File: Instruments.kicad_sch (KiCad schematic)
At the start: 1 part

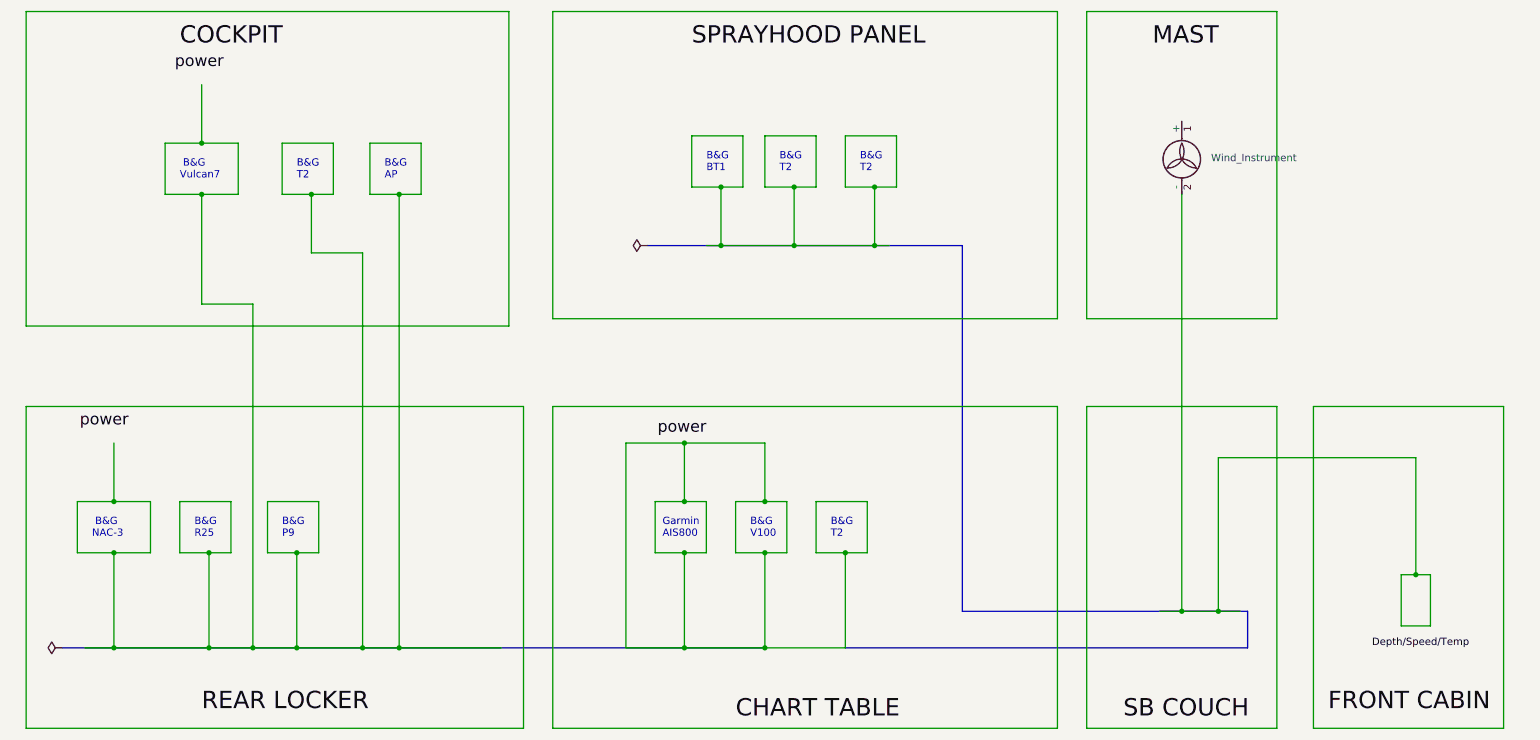
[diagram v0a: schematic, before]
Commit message: BMS Monitor added to network
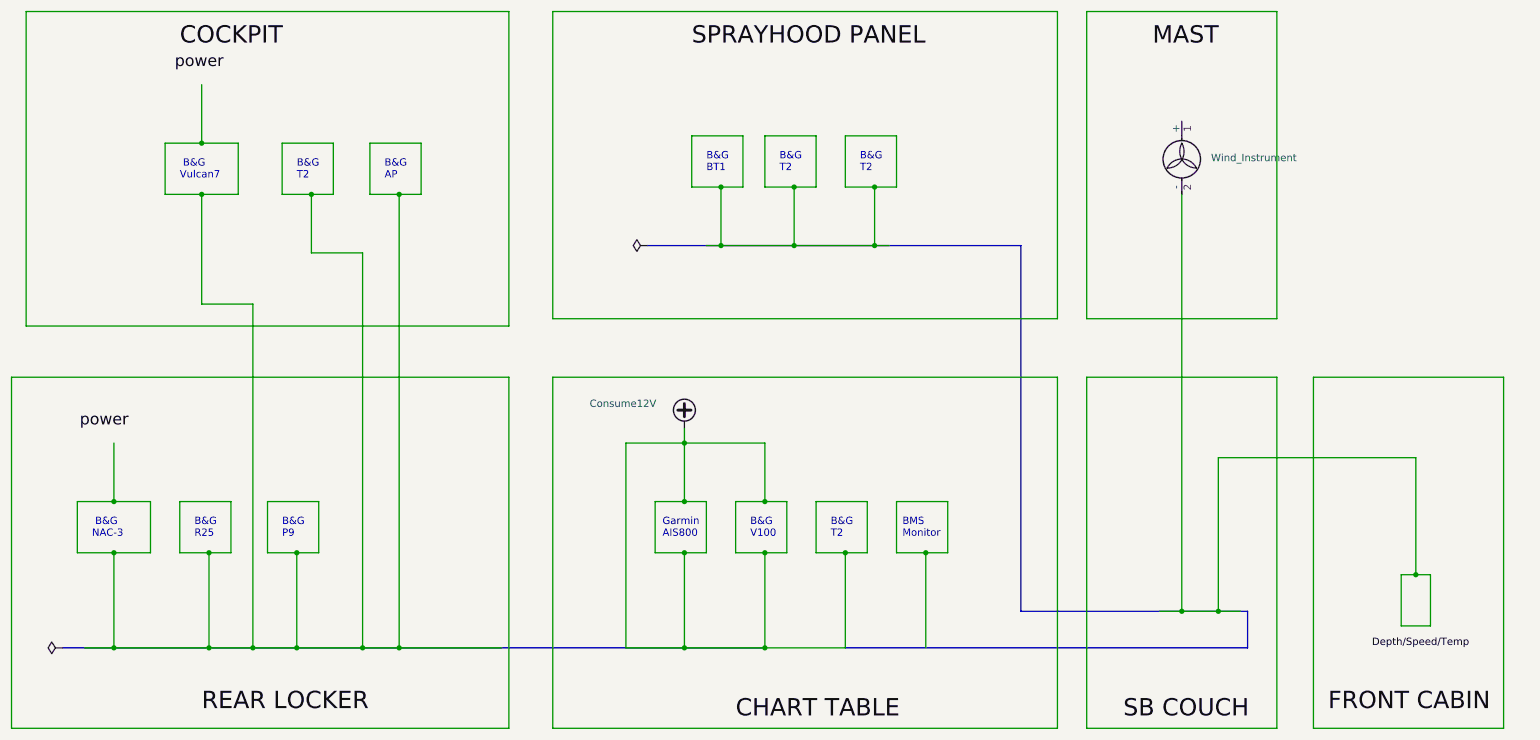
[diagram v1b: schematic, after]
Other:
- note added: "BMS Monitor"
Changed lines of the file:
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@@
 	(title_block
 		(title "Frk Jensen - Instrument cabling")
-		(rev "1.0")
+		(date "2025-06-08")
+		(rev "1.1")
 	)
 	(junction
@@
 	)
 	(junction
+		(at 180.34 115.57)
+		(diameter 0)
+		(color 0 0 0 0)
+	)
+	(junction
 		(at 71.12 115.57)
 		(diameter 0)
@@
 	(wire
 		(pts
+			(xy 175.26 115.57) (xy 180.34 115.57)
+		)
+		(stroke
+			(width 0.4)
+			(type default)
+			(color 1 0 0 1)
+		)
+	)
+	(wire
+		(pts
 			(xy 55.88 115.57) (xy 55.88 132.08)
 		)
@@
 	(bus
 		(pts
-			(xy 186.69 125.73) (xy 186.69 62.23)
+			(xy 196.85 125.73) (xy 196.85 62.23)
 		)
 		(stroke
@@
 	(bus
 		(pts
-			(xy 186.69 125.73) (xy 224.79 125.73)
+			(xy 196.85 125.73) (xy 224.79 125.73)
 		)
 		(stroke
@@
 	(wire
 		(pts
-			(xy 110.49 146.05) (xy 110.49 90.17)
-		)
-		(stroke
-			(width 0)
-			(type dot)
-			(color 0 0 255 1)
+			(xy 107.95 146.05) (xy 107.95 85.09)
+		)
+		(stroke
+			(width 0)
+			(type dot)
+			(color 0 0 255 1)
+		)
+	)
+	(wire
+		(pts
+			(xy 138.43 93.98) (xy 138.43 96.52)
+		)
+		(stroke
+			(width 0)
+			(type default)
 		)
 	)
@@
 	(wire
 		(pts
-			(xy 115.57 90.17) (xy 203.2 90.17)
+			(xy 115.57 85.09) (xy 203.2 85.09)
 		)
 		(stroke
@@
 	(wire
 		(pts
-			(xy 208.28 90.17) (xy 208.28 146.05)
+			(xy 208.28 85.09) (xy 208.28 146.05)
 		)
 		(stroke
@@
 	(wire
 		(pts
-			(xy 203.2 146.05) (xy 203.2 90.17)
+			(xy 203.2 146.05) (xy 203.2 85.09)
 		)
 		(stroke
@@
 	(wire
 		(pts
+			(xy 180.34 115.57) (xy 180.34 132.08)
+		)
+		(stroke
+			(width 1)
+			(type default)
+		)
+	)
+	(wire
+		(pts
 			(xy 166.37 115.57) (xy 170.18 115.57)
 		)
@@
 	(wire
 		(pts
+			(xy 175.26 106.68) (xy 175.26 115.57)
+		)
+		(stroke
+			(width 0.4)
+			(type default)
+			(color 1 0 0 1)
+		)
+	)
+	(wire
+		(pts
 			(xy 208.28 74.93) (xy 241.3 74.93)
 		)
@@
 		)
 	)
+	(wire
+		(pts
+			(xy 175.26 106.68) (xy 184.15 106.68)
+		)
+		(stroke
+			(width 0.4)
+			(type default)
+			(color 1 0 0 1)
+		)
+	)
 	(bus
 		(pts
@@
 	(wire
 		(pts
-			(xy 24.13 146.05) (xy 110.49 146.05)
+			(xy 21.59 146.05) (xy 107.95 146.05)
 		)
 		(stroke
@@
 	(wire
 		(pts
-			(xy 280.67 146.05) (xy 280.67 90.17)
-		)
-		(stroke
-			(width 0)
-			(type dot)
-			(color 0 0 255 1)
-		)
-	)
-	(wire
-		(pts
-			(xy 247.65 90.17) (xy 280.67 90.17)
+			(xy 280.67 146.05) (xy 280.67 85.09)
+		)
+		(stroke
+			(width 0)
+			(type dot)
+			(color 0 0 255 1)
+		)
+	)
+	(wire
+		(pts
+			(xy 247.65 85.09) (xy 280.67 85.09)
 		)
 		(stroke
@@
 	(bus
 		(pts
-			(xy 171.45 62.23) (xy 186.69 62.23)
+			(xy 171.45 62.23) (xy 196.85 62.23)
 		)
 		(stroke
@@
 	(wire
 		(pts
-			(xy 24.13 90.17) (xy 24.13 146.05)
+			(xy 21.59 85.09) (xy 21.59 146.05)
 		)
 		(stroke
@@
 	(wire
 		(pts
-			(xy 247.65 90.17) (xy 247.65 146.05)
+			(xy 247.65 85.09) (xy 247.65 146.05)
 		)
 		(stroke
@@
 	(wire
 		(pts
-			(xy 208.28 90.17) (xy 241.3 90.17)
-		)
-		(stroke
-			(width 0)
-			(type dot)
-			(color 0 0 255 1)
-		)
-	)
-	(wire
-		(pts
-			(xy 24.13 90.17) (xy 110.49 90.17)
+			(xy 208.28 85.09) (xy 241.3 85.09)
+		)
+		(stroke
+			(width 0)
+			(type dot)
+			(color 0 0 255 1)
+		)
+	)
+	(wire
+		(pts
+			(xy 21.59 85.09) (xy 107.95 85.09)
 		)
 		(stroke
@@
 	(wire
 		(pts
+			(xy 184.15 106.68) (xy 184.15 115.57)
+		)
+		(stroke
+			(width 0.4)
+			(type default)
+			(color 1 0 0 1)
+		)
+	)
+	(wire
+		(pts
 			(xy 152.4 43.18) (xy 161.29 43.18)
 		)
@@
 	(wire
 		(pts
+			(xy 180.34 115.57) (xy 184.15 115.57)
+		)
+		(stroke
+			(width 0.4)
+			(type default)
+			(color 1 0 0 1)
+		)
+	)
+	(wire
+		(pts
 			(xy 265.43 119.38) (xy 267.97 119.38)
 		)
@@
 	(wire
 		(pts
-			(xy 115.57 90.17) (xy 115.57 146.05)
+			(xy 115.57 85.09) (xy 115.57 146.05)
 		)
 		(stroke
@@
 	(wire
 		(pts
-			(xy 241.3 146.05) (xy 241.3 90.17)
+			(xy 241.3 146.05) (xy 241.3 85.09)
 		)
 		(stroke
@@
 		)
 	)
+	(text "BMS\nMonitor"
+		(exclude_from_sim no)
+		(at 176.276 113.03 0)
+		(effects
+			(font
+				(size 1.27 1.27)
+			)
+			(justify left bottom)
+		)
+	)
 	(text "B&G\nT2"
 		(exclude_from_sim no)
@@
 			)
 			(justify left bottom)
-		)
-	)
-	(label "power"
-		(at 142.24 95.25 180)
-		(effects
-			(font
-				(size 2 2)
-			)
-			(justify right bottom)
 		)
 	)
@@
 					(unit 1)
 				)
+			)
+		)
+	)
+	(symbol
+		(lib_id "power:+VDC")
+		(at 138.43 93.98 0)
+		(unit 1)
+		(exclude_from_sim no)
+		(in_bom yes)
+		(on_board yes)
+		(dnp no)
+		(property "Reference" "#PWR1"
+			(at 138.43 96.52 0)
+			(effects
+				(font
+					(size 1.27 1.27)
+				)
+				(hide yes)
+			)
+		)
+		(property "Value" "Consume12V"
+			(at 127.762 89.662 0)
+			(effects
+				(font
+					(size 1.27 1.27)
+				)
+			)
+		)
+		(property "Footprint" ""
+			(at 138.43 93.98 0)
+			(effects
+				(font
+					(size 1.27 1.27)
+				)
+				(hide yes)
+			)
+		)
+		(property "Datasheet" ""
+			(at 138.43 93.98 0)
+			(effects
+				(font
+					(size 1.27 1.27)
+				)
+				(hide yes)
+			)
+		)
+		(property "Description" "Power symbol creates a global label with name \"+VDC\""
+			(at 138.43 93.98 0)
+			(effects
+				(font
+					(size 1.27 1.27)
+				)
+				(hide yes)
+			)
+		)
+		(pin "1"
+		)
+		(instances
+			(project ""
+				(path "/07a4a55b-24ff-4c77-909b-7d2015c2831c"
+					(reference "#PWR1")
+					(unit 1)
+				)
